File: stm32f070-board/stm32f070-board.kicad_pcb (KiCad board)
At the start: 2 copper layers, 69.6 x 31.5 mm, 39 parts, among them J1 USB_B_Micro, J2 USB_B_Micro, J3 Conn_01x05_Male, SW1 SW_DPDT_x2, SW2 SW_Push, SW3 SW_Push, U1 CH340G, U2 STM32F070F6P6, U3 MCP9700AT-ETT, U4 Si7055-A20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

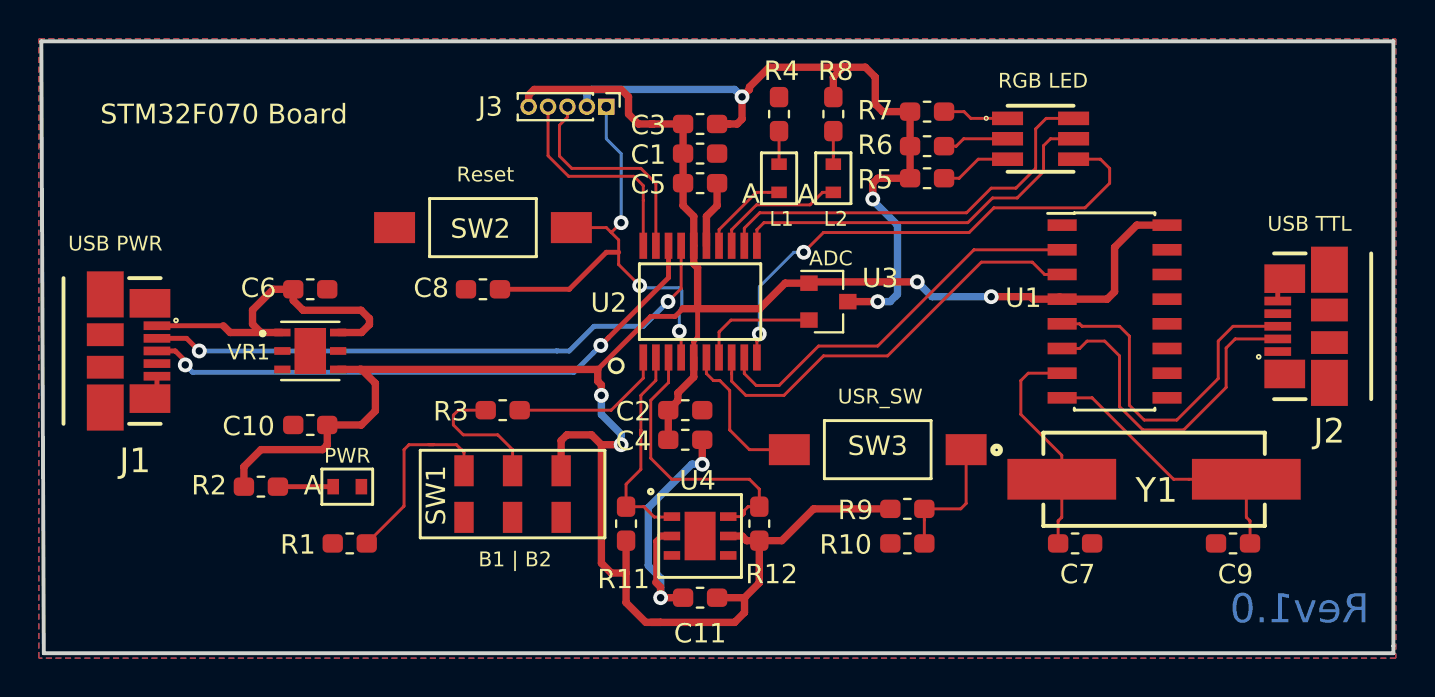
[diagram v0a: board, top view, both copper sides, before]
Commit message: added 5v connection to usb jack of ch340(serail converter ic), updated track widths
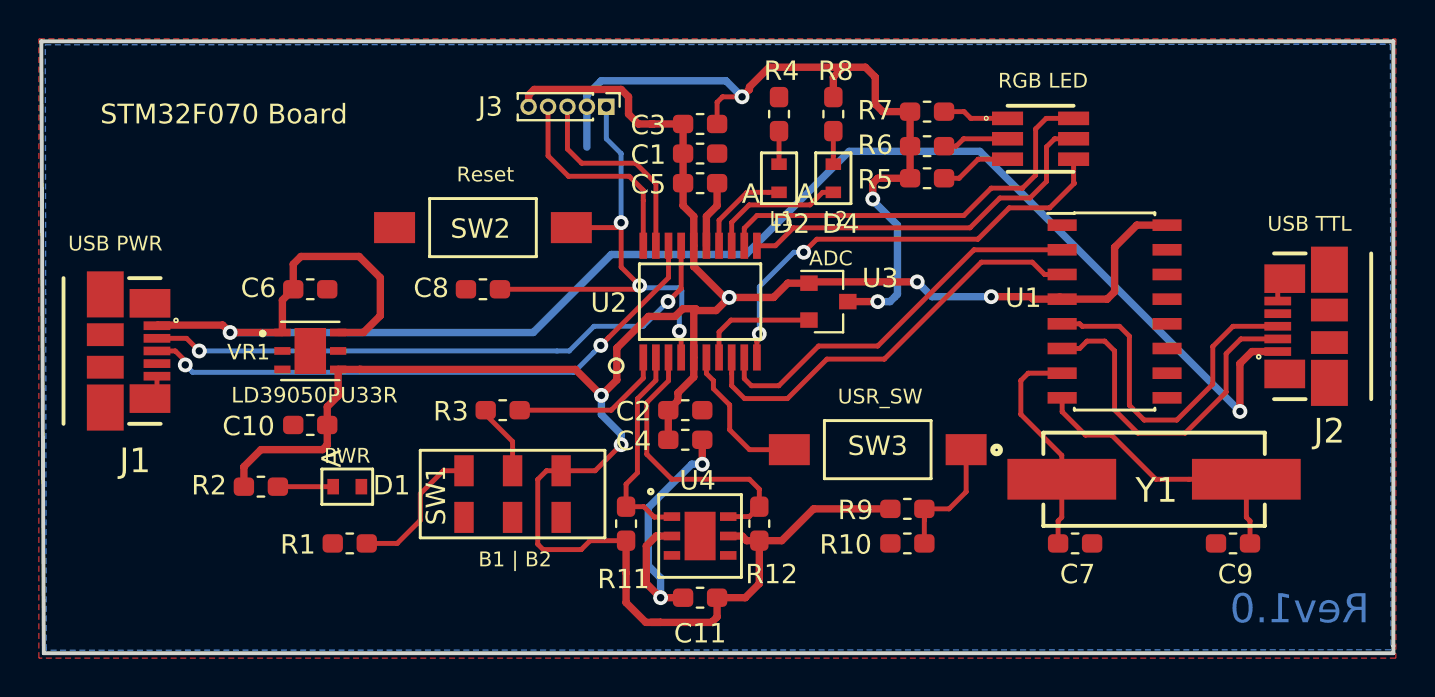
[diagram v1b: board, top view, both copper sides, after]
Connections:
- C6 pad 1: Net-(C6-Pad1) -> +5V
- J1 pad 1: Net-(C6-Pad1) -> +5V
- J2 pad 1: Net-(J2-Pad1) -> +5V
- VR1 pad 1: Net-(C6-Pad1) -> +5V
- VR1 pad 6: Net-(C6-Pad1) -> +5V
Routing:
- net +5V: track 0.00 -> 86.0 mm, vias 0 -> 2
- net Net-(C6-Pad1): track 17.4 -> 0.00 mm
- net Net-(D3-Pad4): track 26.7 -> 23.4 mm
- net Net-(R3-Pad2): track 6.94 -> 3.69 mm
- net GND: track 60.0 -> 62.9 mm
- net Net-(R1-Pad2): track 10.5 -> 7.65 mm
- net VCC: track 129.6 -> 128.0 mm, vias 4 -> 5
- net /PA19: track 11.5 -> 10.7 mm
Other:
- net class Default: clearance 0.254 -> 0.127
- net class GND_TRACK: clearance 0.254 -> 0.127
- net class VCC_TRACK: clearance 0.254 -> 0.127
- rule trace_clearance: 0.254 -> 0.127

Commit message: added cacpacitor near usb jack - ch340 side
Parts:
- added C12: 1uF, Capacitor_SMD:C_0603_1608Metric_Pad1.05x0.95mm_HandSolder, F.Cu at (159.4, 107.6)
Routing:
- net +5V: track 86.0 -> 88.5 mm
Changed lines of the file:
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@@
     (thickness 1.6)
     (drawings 18)
-    (tracks 393)
+    (tracks 395)
     (zones 0)
-    (modules 39)
+    (modules 40)
     (nets 46)
   )
@@
     (35 F.Paste user hide)
     (36 B.SilkS user hide)
-    (37 F.SilkS user hide)
+    (37 F.SilkS user)
     (38 B.Mask user hide)
     (39 F.Mask user hide)
@@
     (add_net VCC)
   )
+  (module Capacitor_SMD:C_0603_1608Metric_Pad1.05x0.95mm_HandSolder (layer F.Cu)
+    (at 159.371 107.6452)
+    (descr "Capacitor SMD 0603 (1608 Metric), square (rectangular) end terminal, IPC_7351 nominal with elongated pad for handsoldering. (Body size source: http://www.tortai-tech.com/upload/download/2011102023233369053.pdf), generated with kicad-footprint-generator")
+    (tags "capacitor handsolder")
+    (attr smd)
+    (fp_text reference C12 (at 1.8682 1.4732) (layer F.SilkS)
+      (effects (font (size 1 1) (thickness 0.15)))
+    )
+    (fp_text value 1uF (at 0 1.43) (layer F.Fab)
+      (effects (font (size 1 1) (thickness 0.15)))
+    )
+    (fp_line (start -0.8 0.4) (end -0.8 -0.4) (layer F.Fab) (width 0.1))
+    (fp_line (start -0.8 -0.4) (end 0.8 -0.4) (layer F.Fab) (width 0.1))
+    (fp_line (start 0.8 -0.4) (end 0.8 0.4) (layer F.Fab) (width 0.1))
+    (fp_line (start 0.8 0.4) (end -0.8 0.4) (layer F.Fab) (width 0.1))
+    (fp_line (start -0.171267 -0.51) (end 0.171267 -0.51) (layer F.SilkS) (width 0.12))
+    (fp_line (start -0.171267 0.51) (end 0.171267 0.51) (layer F.SilkS) (width 0.12))
+    (fp_line (start -1.65 0.73) (end -1.65 -0.73) (layer F.CrtYd) (width 0.05))
+    (fp_line (start -1.65 -0.73) (end 1.65 -0.73) (layer F.CrtYd) (width 0.05))
+    (fp_line (start 1.65 -0.73) (end 1.65 0.73) (layer F.CrtYd) (width 0.05))
+    (fp_line (start 1.65 0.73) (end -1.65 0.73) (layer F.CrtYd) (width 0.05))
+    (fp_text user %R (at 0 0) (layer F.Fab)
+      (effects (font (size 0.4 0.4) (thickness 0.06)))
+    )
+    (pad 1 smd roundrect (at -0.875 0) (size 1.05 0.95) (layers F.Cu F.Paste F.Mask) (roundrect_rratio 0.25)
+      (net 45 +5V))
+    (pad 2 smd roundrect (at 0.875 0) (size 1.05 0.95) (layers F.Cu F.Paste F.Mask) (roundrect_rratio 0.25)
+      (net 2 GND))
+    (model ${KISYS3DMOD}/Capacitor_SMD.3dshapes/C_0603_1608Metric.wrl
+      (at (xyz 0 0 0))
+      (scale (xyz 1 1 1))
+      (rotate (xyz 0 0 0))
+    )
+  )
   (module stm32f070-board:TSSOP20_P0.65mm (layer F.Cu)
     (at 128.651 101.0285)
@@
     (tags LED)
     (attr smd)
-    (fp_text reference D3 (at 4.445 0.0635) (layer F.SilkS) hide
+    (fp_text reference D3 (at 4.445 0.0635) (layer F.Fab) hide
       (effects (font (size 1.27 1.27) (thickness 0.254)))
     )
-    (fp_text value LED_RGB (at 0.127 -2.9845) (layer F.SilkS) hide
+    (fp_text value LED_RGB (at 0.127 -2.9845) (layer F.Fab) hide
       (effects (font (size 1.27 1.27) (thickness 0.254)))
     )
@@
       (effects (font (size 1.27 1.27) (thickness 0.254)))
     )
-    (fp_text value USB_B_Micro (at -5.6515 2.413 180) (layer F.SilkS) hide
+    (fp_text value USB_B_Micro (at -10.4013 6.5024 180) (layer F.Fab) hide
       (effects (font (size 1.27 1.27) (thickness 0.254)))
     )
@@
     (tags Connector)
     (attr smd)
-    (fp_text reference J2 (at 5.3975 2.159) (layer F.SilkS)
+    (fp_text reference J2 (at 5.1943 0.4064) (layer F.SilkS)
       (effects (font (size 1.27 1.27) (thickness 0.254)))
     )
-    (fp_text value USB_B_Micro (at -0.313 3.58 270) (layer F.SilkS) hide
+    (fp_text value USB_B_Micro (at -7.1247 5.8166) (layer F.Fab) hide
       (effects (font (size 1.27 1.27) (thickness 0.254)))
     )
@@
   (segment (start 104.079001 102.237501) (end 100.725999 102.237501) (width 0.381) (layer F.Cu) (net 45))
   (segment (start 104.46 102.6185) (end 104.079001 102.237501) (width 0.381) (layer F.Cu) (net 45))
+  (segment (start 157.5308 106.68) (end 158.496 107.6452) (width 0.381) (layer F.Cu) (net 45))
+  (segment (start 156.4386 106.68) (end 157.5308 106.68) (width 0.381) (layer F.Cu) (net 45))
   (zone (net 2) (net_name GND) (layer F.Cu) (hatch edge 0.508)
     (connect_pads (clearance 0.508))

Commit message: made final changes to the pcb layout
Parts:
- moved C12 4.10 mm to (161.8, 111.0), turned to 270 degrees
- moved C7 2.10 mm to (148.0, 115.6)
- moved C9 2.10 mm to (156.1, 115.6)
- moved Y1 1.41 mm to (151.9, 111.6)
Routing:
- net +5V: track 88.5 -> 94.6 mm
- net Net-(C7-Pad1): track 11.6 -> 14.5 mm
- net Net-(C9-Pad1): track 15.0 -> 17.7 mm
- net GND: track 62.9 -> 60.8 mm
- net /ToDebugConnector: track 25.7 -> 24.6 mm
- net /USB_D+: track 30.6 -> 31.3 mm
- net VCC: track 128.0 -> 127.4 mm
